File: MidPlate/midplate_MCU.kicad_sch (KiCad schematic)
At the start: 12 parts, among them U1 STM32F103C8Tx, U2 MCP2551-I-SN, Y1 Crystal_Small, Y2 Crystal_Small

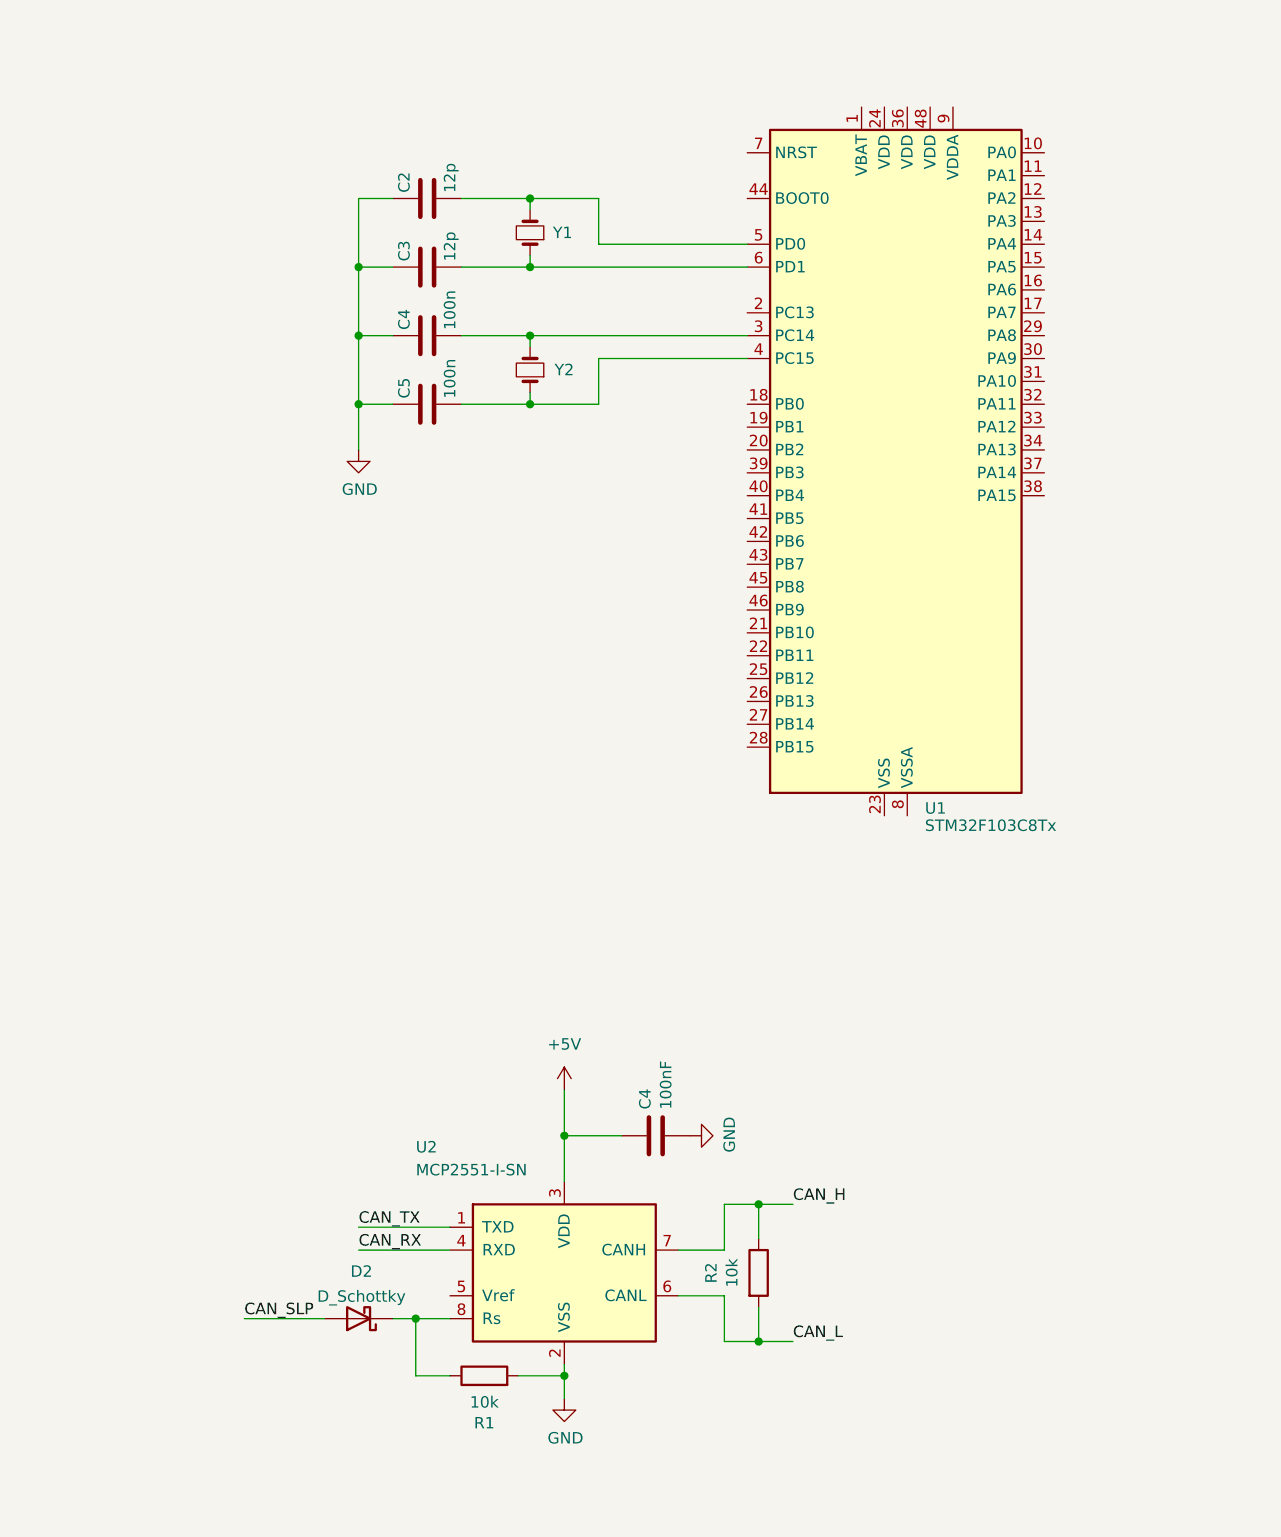
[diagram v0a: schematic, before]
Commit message: added OPi Zero2 symbol and subsheet to midplate
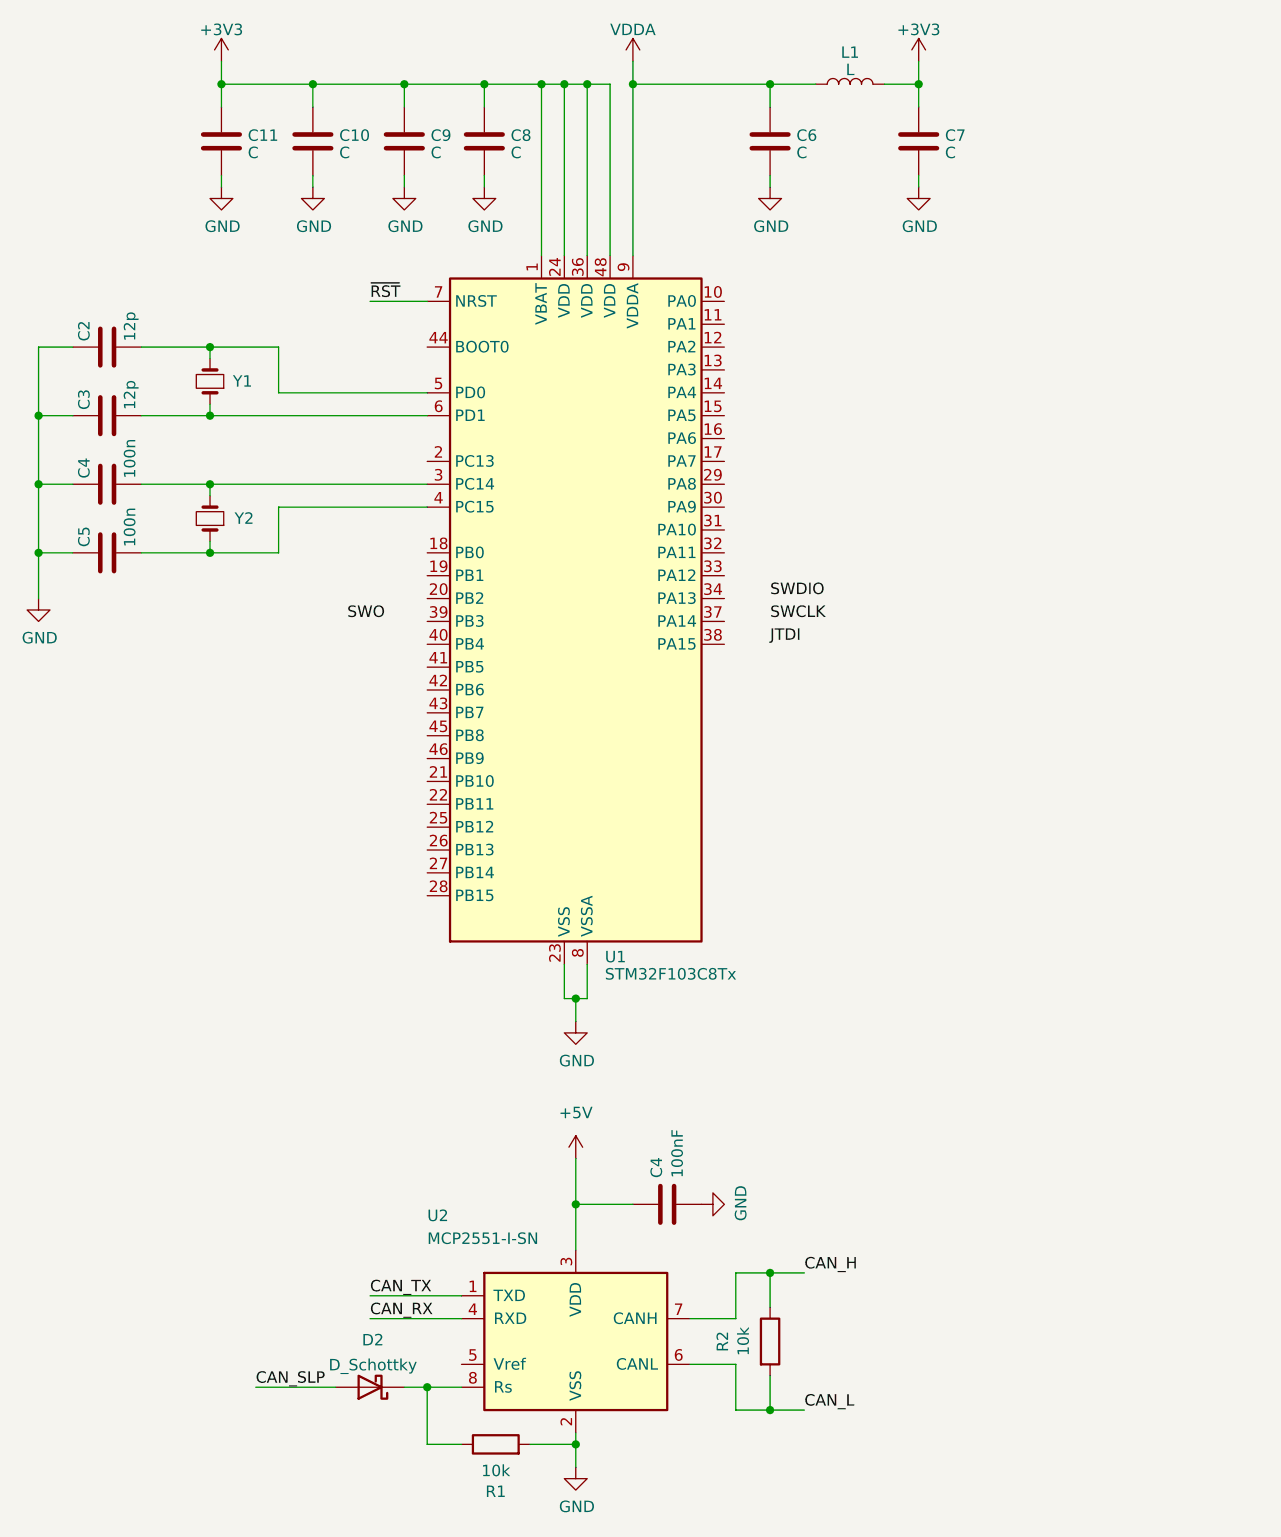
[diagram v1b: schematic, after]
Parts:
- added C10, C11, C6, C7, C8, C9: C, symbol Device:C
- added L1: L, symbol Device:L
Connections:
- net GND: now also U1.23 (VSS), U1.35 (VSS), U1.47 (VSS), U1.8 (VSSA), C10.2, C11.2, C6.2, C7.2, C8.2, C9.2
- net +3V3: now reaches U1.1 (VBAT)
- net +3V3: now also U1.24 (VDD), U1.36 (VDD), U1.48 (VDD), C10.1, C11.1, C7.1, C8.1, C9.1, L1.2
- net ~{RST}: now reaches U1.7 (NRST)
- net VDDA: now reaches U1.9 (VDDA)
- net VDDA: now also C6.1, L1.1
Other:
- moved on the sheet: C2, C3, C4, C5, D2, R1, R2, U1, U2, Y1, Y2

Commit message: update to power board and midplate schematics
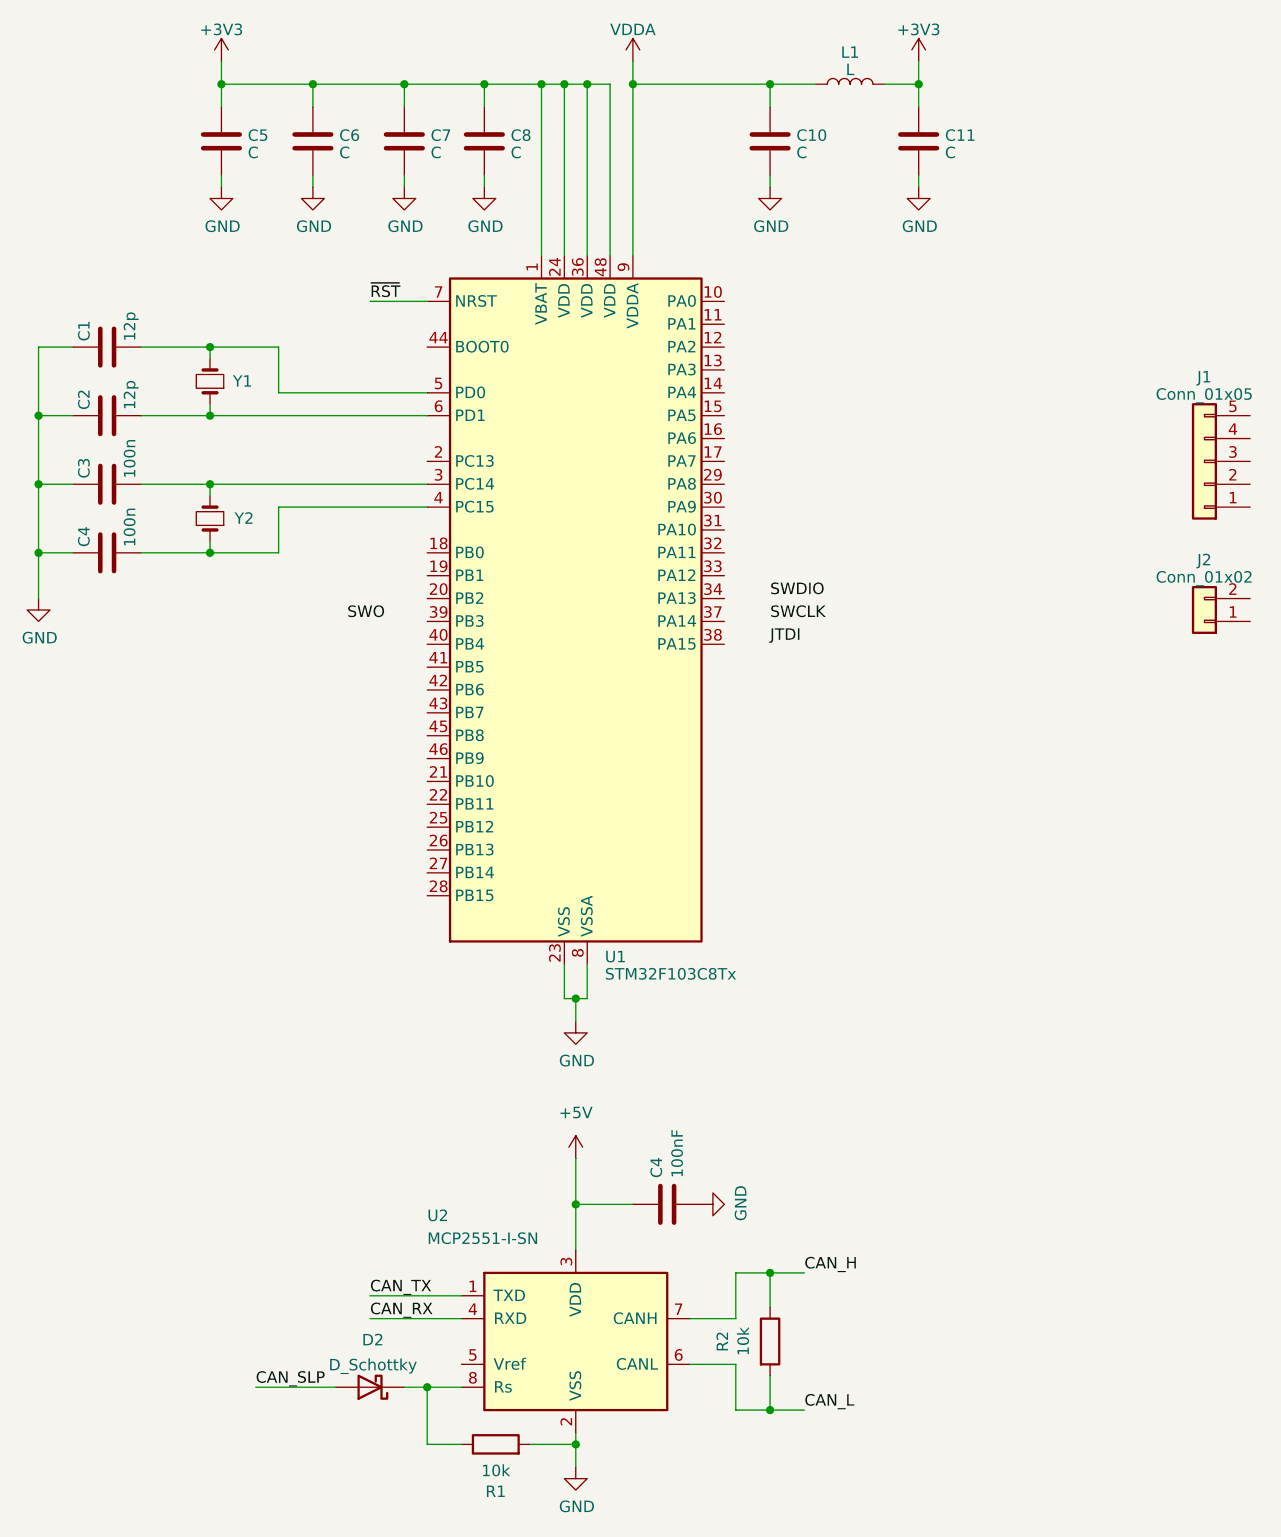
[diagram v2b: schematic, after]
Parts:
- added J1: Conn_01x05, symbol Connector_Generic:Conn_01x05
- added J2: Conn_01x02, symbol Connector_Generic:Conn_01x02
- renumbered C2 to C1, C6 to C10, C7 to C11, C3 to C2, C4 to C3, C5 to C4, C11 to C5, C10 to C6, C9 to C7

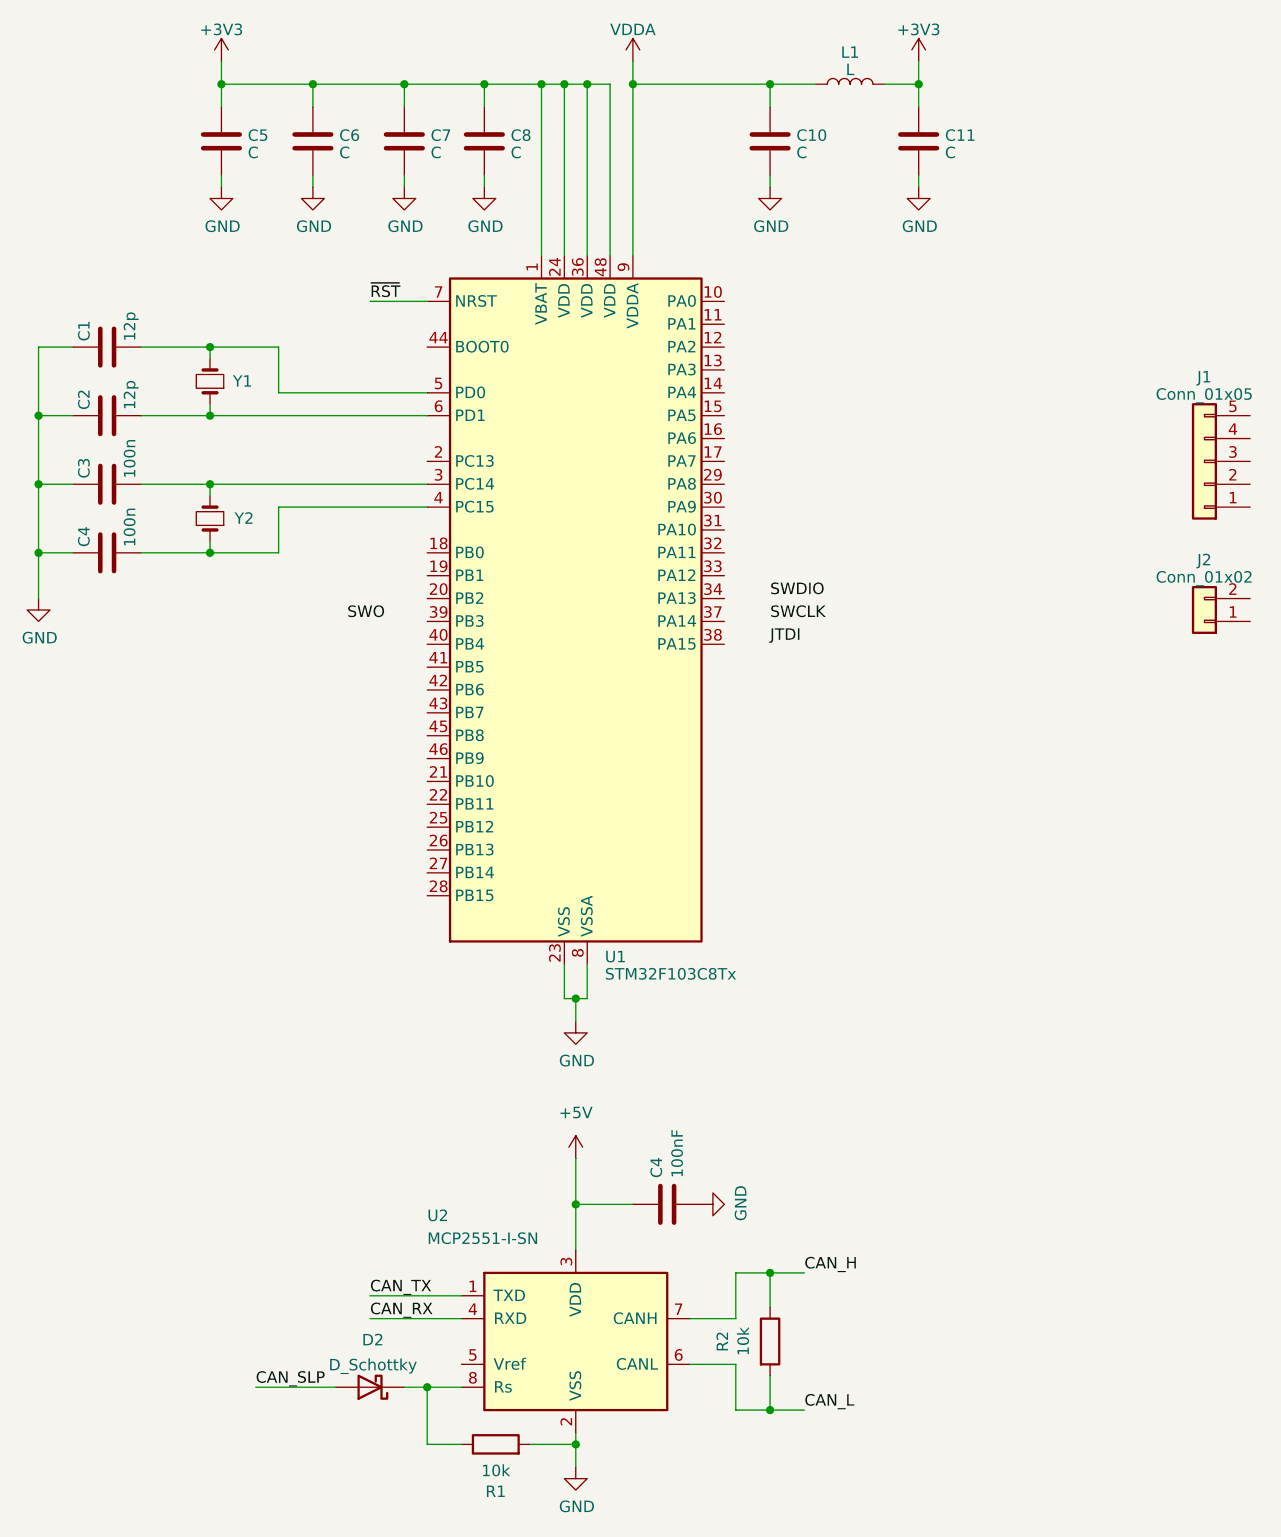
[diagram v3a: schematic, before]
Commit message: powerboard HV powerpillars + midplate
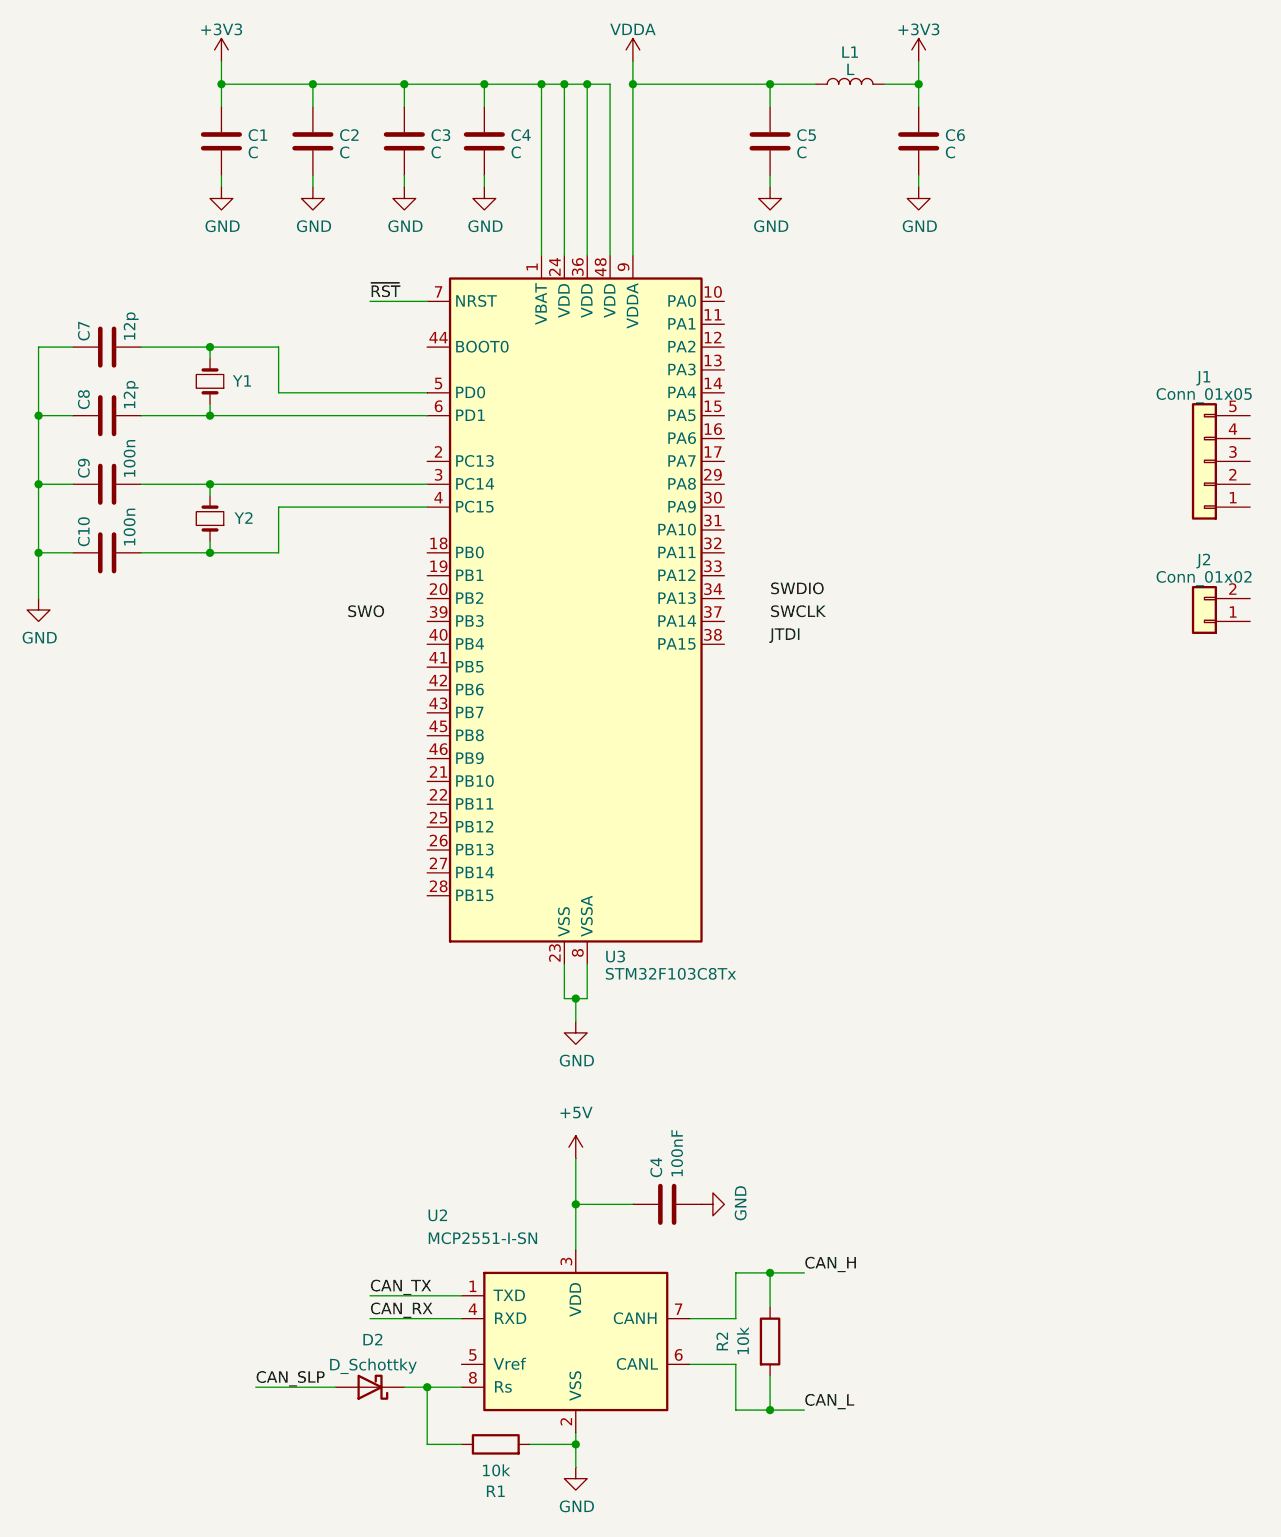
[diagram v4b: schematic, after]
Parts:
- renumbered C5 to C1, C4 to C10, C6 to C2, C7 to C3, C8 to C4, C10 to C5, C11 to C6, C1 to C7, C2 to C8, C3 to C9, U1 to U3
